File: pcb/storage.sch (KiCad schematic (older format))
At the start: 31 parts, among them Q300 IRLML6402, Q302 2SK3018, U100 MCIMX7S5EVM08SC, U300 ADP123, U301 W25Q16BV

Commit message: pcb: rev 0.1
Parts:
- removed C305: 2.2uF, Capacitor_SMD:C_0402_1005Metric, symbol Device:C
- removed C306, C307, C308, C309: 220nF, Capacitor_SMD:C_0402_1005Metric, symbol Device:C
- removed C310: 10uF, Capacitor_SMD:C_0603_1608Metric, symbol Device:C
- removed C311, C313: 100nF, Capacitor_SMD:C_0402_1005Metric, symbol Device:C
- removed C312: 4.7uF, Capacitor_SMD:C_0603_1608Metric, symbol Device:C
- removed Q302: 2SK3018, Package_TO_SOT_SMD:SOT-23, symbol Device:Q_NMOS_SGD
- removed R300: 10K, Resistor_SMD:R_0603_1608Metric, symbol Device:R
- removed R306: 560K/1%, Resistor_SMD:R_0603_1608Metric, symbol Device:R
- removed R307: 100K/1%, Resistor_SMD:R_0603_1608Metric, symbol Device:R
- removed R308: 100K, Resistor_SMD:R_0603_1608Metric, symbol Device:R
- removed R309: 487K/1%, Resistor_SMD:R_0603_1608Metric, symbol Device:R
- removed U100: MCIMX7S5EVM08SC, footprints:BGA-541_25x25_19.0x19.0mm, symbol symbols:MCIMX7S5EVM08SC
- removed U300: ADP123, Package_TO_SOT_SMD:TSOT-23-5, symbol Regulator_Linear:ADP7142AUJZ
- removed U301: W25Q16BV, Package_SON:WSON-8-1EP_6x5mm_P1.27mm_EP3.4x4mm, symbol symbols:W25Q16BV
- added U300: TXS0108EPW, Package_SO:TSSOP-20_4.4x6.5mm_P0.65mm, symbol symbols:TXS0108EPW
- C303: value 4.7uF -> 100nF; footprint Capacitor_SMD:C_0603_1608Metric -> Capacitor_SMD:C_0402_1005Metric
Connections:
- net +1V8: now also U300.10 (OE), U300.2 (VCCA); no longer C304.1
- net +3V3: now also C304.2, R301.1, R302.1, U300.19 (VCCB)
- net GND: now also U300.11 (GND); no longer C304.2
- net SD1_CD renamed ~SD0_CD
- net SD1_CLK renamed SD_CLK
- net SD_CLK: now also U300.17 (B3)
- net SD1_CMD renamed SD_CMD
- net SD_CMD: now also U300.18 (B2)
- net SD1_DATA0 renamed SD_D0
- net SD_D0: now also U300.14 (B6)
- net SD1_DATA1 renamed SD_D1
- net SD_D1: now also U300.13 (B7)
- net SD1_DATA2 renamed SD_D2
- net SD_D2: now also U300.16 (B4)
- net SD1_DATA3 renamed SD_D3
- net SD_D3: now also U300.15 (B5)
- net ~SD_PWR_EN renamed SD_PWR_EN
- net SD_PWR_EN: now also U300.20 (B1)
- new net SD0_CLK: U300.4 (A3)
- new net SD0_CMD: U300.3 (A2)
- new net SD0_D0: U300.7 (A6)
- new net SD0_D1: U300.8 (A7)
- new net SD0_D2: U300.5 (A4)
- new net SD0_D3: U300.6 (A5)
- new net ~SD0_PWR_EN: U300.1 (A1)
- no-connect marks 23 -> 0
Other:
- note removed: "Configure as 32kHz clock output"
- note removed: "FB = 0.5V, use 560K/487K/100K\nFB = 0.8V, use 499K/330K/160K\nFB = 1.0V, use 464K/243K/200K"
- note removed: "To Audio DAC\n"
- note removed: "To WiFi&BT"
- moved on the sheet: R303

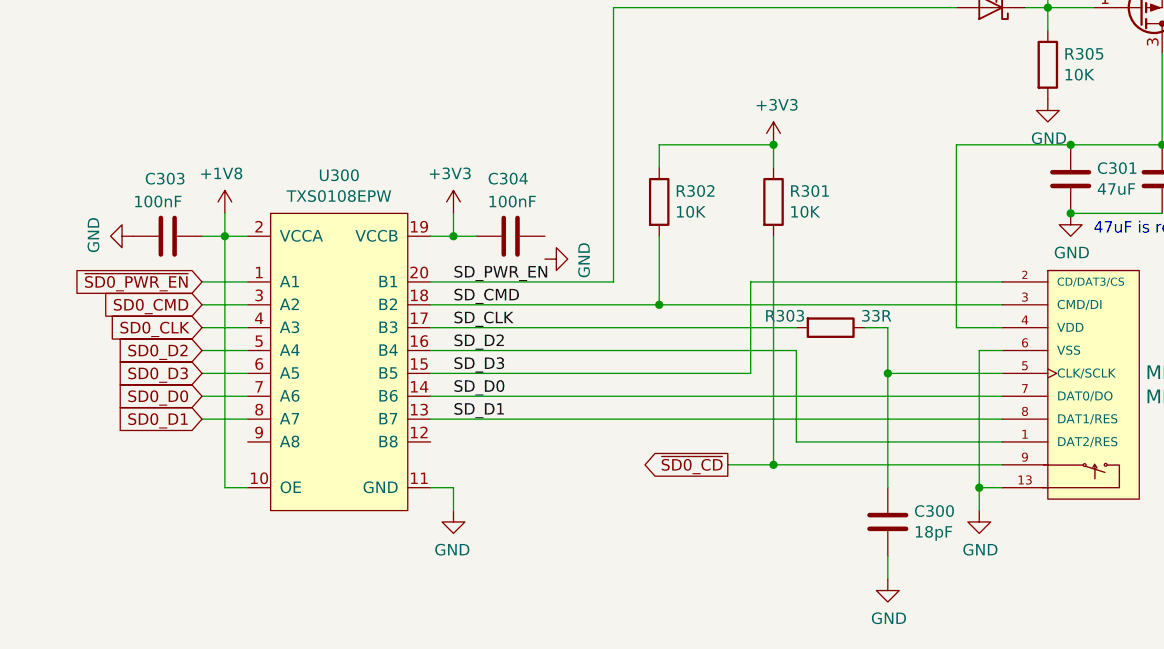
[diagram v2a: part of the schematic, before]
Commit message: pcb: fixing voltage domain
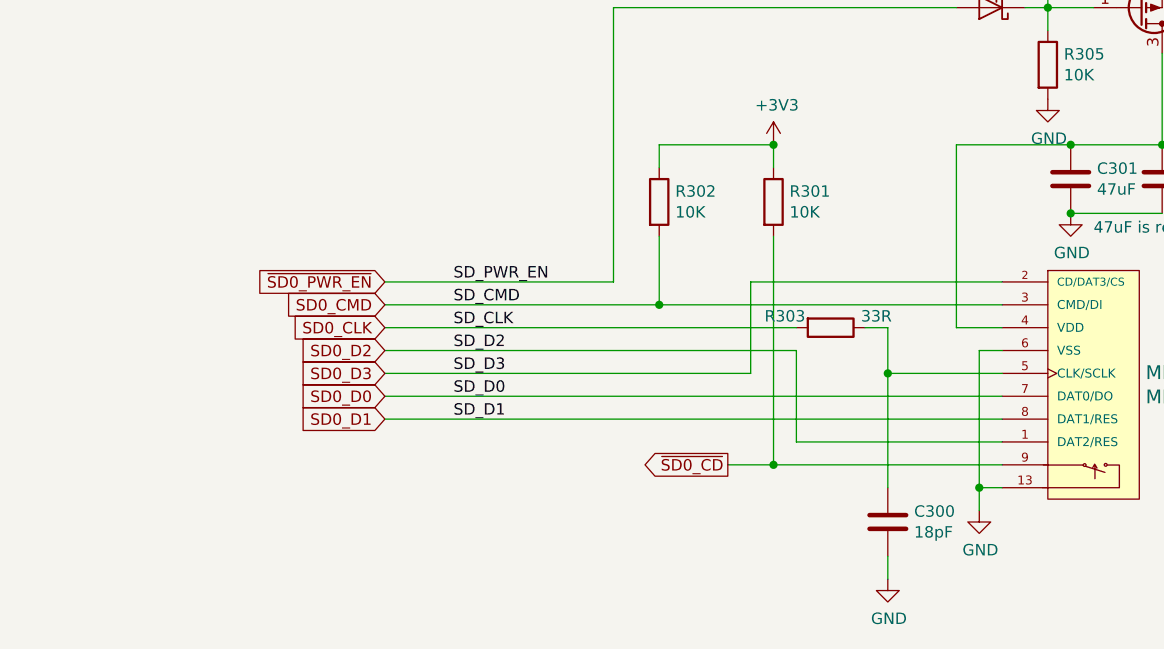
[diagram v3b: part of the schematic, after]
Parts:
- removed C303, C304: 100nF, Capacitor_SMD:C_0402_1005Metric, symbol Device:C
- removed U300: TXS0108EPW, Package_SO:TSSOP-20_4.4x6.5mm_P0.65mm, symbol symbols:TXS0108EPW
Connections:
- net SD_CLK is gone; now on net SD0_CLK: R303.2
- net SD_CMD is gone; now on net SD0_CMD: MICRO_SD300.3 (CMD/DI), R302.2
- net SD_D0 is gone; now on net SD0_D0: MICRO_SD300.7 (DAT0/DO)
- net SD_D1 is gone; now on net SD0_D1: MICRO_SD300.8 (DAT1/RES)
- net SD_D2 is gone; now on net SD0_D2: MICRO_SD300.1 (DAT2/RES)
- net SD_D3 is gone; now on net SD0_D3: MICRO_SD300.2 (CD/DAT3/CS)
- net SD_PWR_EN is gone; now on net ~SD0_PWR_EN: D300.2 (A)
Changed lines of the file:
@@
 	1    0    0    -1
 $EndComp
-Text GLabel 3900 3300 0    50   Input ~ 0
+Text GLabel 4700 3300 0    50   Input ~ 0
 ~SD0_PWR_EN
 Wire Wire Line
@@
 Wire Wire Line
 	6400 2700 6400 2800
-Text GLabel 3900 3500 0    50   Input ~ 0
+Text GLabel 4700 3500 0    50   Input ~ 0
 SD0_CLK
-Text GLabel 3900 3400 0    50   Input ~ 0
+Text GLabel 4700 3400 0    50   Input ~ 0
 SD0_CMD
-Text GLabel 3900 3800 0    50   Input ~ 0
+Text GLabel 4700 3800 0    50   Input ~ 0
 SD0_D0
-Text GLabel 3900 3900 0    50   Input ~ 0
+Text GLabel 4700 3900 0    50   Input ~ 0
 SD0_D1
-Text GLabel 3900 3600 0    50   Input ~ 0
+Text GLabel 4700 3600 0    50   Input ~ 0
 SD0_D2
-Text GLabel 3900 3700 0    50   Input ~ 0
+Text GLabel 4700 3700 0    50   Input ~ 0
 SD0_D3
 Text GLabel 6200 4100 0    50   Output ~ 0
@@
 $EndComp
 Connection ~ 6400 2700
-$Comp
-L symbols:TXS0108EPW U?
-U 1 1 5D7F7878
-P 4500 3300
-AR Path="/5D438133/5D7F7878" Ref="U?"  Part="1"
-AR Path="/5DB2122B/5D7F7878" Ref="U300"  Part="1"
-F 0 "U300" H 4500 3765 50  0000 C CNN
-F 1 "TXS0108EPW" H 4500 3674 50  0000 C CNN
-F 2 "Package_SO:TSSOP-20_4.4x6.5mm_P0.65mm" H 4500 3300 50  0001 C CNN
-F 3 "" H 4500 3300 50  0001 C CNN
-	1    4500 3300
-	1    0    0    -1
-$EndComp
-$Comp
-L power:+3V3 #PWR?
-U 1 1 5D7F7886
-P 5000 3000
-AR Path="/5D438133/5D7F7886" Ref="#PWR?"  Part="1"
-AR Path="/5DB2122B/5D7F7886" Ref="#PWR0109"  Part="1"
-F 0 "#PWR0109" H 5000 2850 50  0001 C CNN
-F 1 "+3V3" H 5015 3173 50  0000 C CNN
-F 2 "" H 5000 3000 50  0001 C CNN
-F 3 "" H 5000 3000 50  0001 C CNN
-	1    5000 3000
-	-1   0    0    -1
-$EndComp
-Wire Wire Line
-	5000 3000 5000 3100
-Wire Wire Line
-	5000 3100 4900 3100
-$Comp
-L power:GND #PWR?
-U 1 1 5D7F788E
-P 5000 4300
-AR Path="/5D438133/5D7F788E" Ref="#PWR?"  Part="1"
-AR Path="/5DB2122B/5D7F788E" Ref="#PWR0110"  Part="1"
-F 0 "#PWR0110" H 5000 4050 50  0001 C CNN
-F 1 "GND" H 5005 4127 50  0000 C CNN
-F 2 "" H 5000 4300 50  0001 C CNN
-F 3 "" H 5000 4300 50  0001 C CNN
-	1    5000 4300
-	-1   0    0    -1
-$EndComp
-Wire Wire Line
-	4900 4200 5000 4200
-Wire Wire Line
-	5000 4200 5000 4300
-$Comp
-L Device:C C?
-U 1 1 5D7F7896
-P 5250 3100
-AR Path="/5D438133/5D7F7896" Ref="C?"  Part="1"
-AR Path="/5DB2122B/5D7F7896" Ref="C304"  Part="1"
-F 0 "C304" V 5500 3000 50  0000 L CNN
-F 1 "100nF" V 5400 3000 50  0000 L CNN
-F 2 "Capacitor_SMD:C_0402_1005Metric" H 5288 2950 50  0001 C CNN
-F 3 "~" H 5250 3100 50  0001 C CNN
-	1    5250 3100
-	0    1    -1   0
-$EndComp
-Wire Wire Line
-	5100 3100 5000 3100
-Connection ~ 5000 3100
-$Comp
-L power:GND #PWR?
-U 1 1 5D7F789E
-P 5400 3200
-AR Path="/5D438133/5D7F789E" Ref="#PWR?"  Part="1"
-AR Path="/5DB2122B/5D7F789E" Ref="#PWR0111"  Part="1"
-F 0 "#PWR0111" H 5400 2950 50  0001 C CNN
-F 1 "GND" H 5405 3027 50  0000 C CNN
-F 2 "" H 5400 3200 50  0001 C CNN
-F 3 "" H 5400 3200 50  0001 C CNN
-	1    5400 3200
-	0    -1   1    0
-$EndComp
-$Comp
-L power:+1V8 #PWR?
-U 1 1 5D80C6E8
-P 4000 3000
-AR Path="/5D438133/5D80C6E8" Ref="#PWR?"  Part="1"
-AR Path="/5DB2122B/5D80C6E8" Ref="#PWR0114"  Part="1"
-F 0 "#PWR0114" H 4000 2850 50  0001 C CNN
-F 1 "+1V8" H 4015 3173 50  0000 C CNN
-F 2 "" H 4000 3000 50  0001 C CNN
-F 3 "" H 4000 3000 50  0001 C CNN
-	1    4000 3000
-	-1   0    0    -1
-$EndComp
-Wire Wire Line
-	4100 3100 4000 3100
-Wire Wire Line
-	4000 3100 4000 3000
-Wire Wire Line
-	4000 4200 4000 3100
-Connection ~ 4000 3100
-$Comp
-L Device:C C?
-U 1 1 5D80C6F2
-P 3750 3100
-AR Path="/5D438133/5D80C6F2" Ref="C?"  Part="1"
-AR Path="/5DB2122B/5D80C6F2" Ref="C303"  Part="1"
-F 0 "C303" V 4000 3000 50  0000 L CNN
-F 1 "100nF" V 3900 2950 50  0000 L CNN
-F 2 "Capacitor_SMD:C_0402_1005Metric" H 3788 2950 50  0001 C CNN
-F 3 "~" H 3750 3100 50  0001 C CNN
-	1    3750 3100
-	0    1    -1   0
-$EndComp
-Wire Wire Line
-	3900 3100 4000 3100
-$Comp
-L power:GND #PWR?
-U 1 1 5D80C6F9
-P 3600 3100
-AR Path="/5D438133/5D80C6F9" Ref="#PWR?"  Part="1"
-AR Path="/5DB2122B/5D80C6F9" Ref="#PWR0115"  Part="1"
-F 0 "#PWR0115" H 3600 2850 50  0001 C CNN
-F 1 "GND" H 3605 2927 50  0000 C CNN
-F 2 "" H 3600 3100 50  0001 C CNN
-F 3 "" H 3600 3100 50  0001 C CNN
-	1    3600 3100
-	0    1    -1   0
-$EndComp
-Wire Wire Line
-	4000 4200 4100 4200
-Wire Wire Line
-	4900 3300 5700 3300
 Wire Wire Line
 	5700 2100 7200 2100
-Wire Wire Line
-	3900 3300 4100 3300
-Wire Wire Line
-	3900 3400 4100 3400
-Wire Wire Line
-	3900 3500 4100 3500
-Wire Wire Line
-	3900 3600 4100 3600
-Wire Wire Line
-	3900 3700 4100 3700
-Wire Wire Line
-	3900 3800 4100 3800
-Wire Wire Line
-	3900 3900 4100 3900
 Wire Wire Line
 	6200 4100 6400 4100
@@
 Text Label 5000 3700 0    50   ~ 0
 SD_D3
-Wire Wire Line
-	4900 3400 5900 3400
 Connection ~ 5900 3400
 Wire Wire Line
@@
 	5700 3300 5700 2100
 Wire Wire Line
-	4900 3800 7400 3800
-Wire Wire Line
-	4900 3500 6500 3500
-Wire Wire Line
 	6900 3500 6900 3700
 Connection ~ 6900 3700
@@
 	6800 3500 6900 3500
 Wire Wire Line
-	4900 3900 7400 3900
-Wire Wire Line
-	4900 3700 6300 3700
-Wire Wire Line
 	6300 3700 6300 3300
-Wire Wire Line
-	4900 3600 6500 3600
 Wire Wire Line
 	6500 3600 6500 4000
@@
 	6400 3100 6400 4100
 Connection ~ 6400 4100
+Wire Wire Line
+	4700 3300 5700 3300
+Wire Wire Line
+	4700 3400 5900 3400
+Wire Wire Line
+	4700 3500 6500 3500
+Wire Wire Line
+	4700 3600 6500 3600
+Wire Wire Line
+	4700 3700 6300 3700
+Wire Wire Line
+	4700 3800 7400 3800
+Wire Wire Line
+	4700 3900 7400 3900
 $EndSCHEMATC
